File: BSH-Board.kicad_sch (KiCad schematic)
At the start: 57 parts, among them J1 667101210103, J2 MICRO QTZB5.0, SW1 TS-3025-B-C-B, SW2 TS-3025-B-C-B, U1 ESP32-C6-MINI-1-N4, U2 AP63203WU, U3 NCP715SQ50T2G, U4 TXS0102DQER

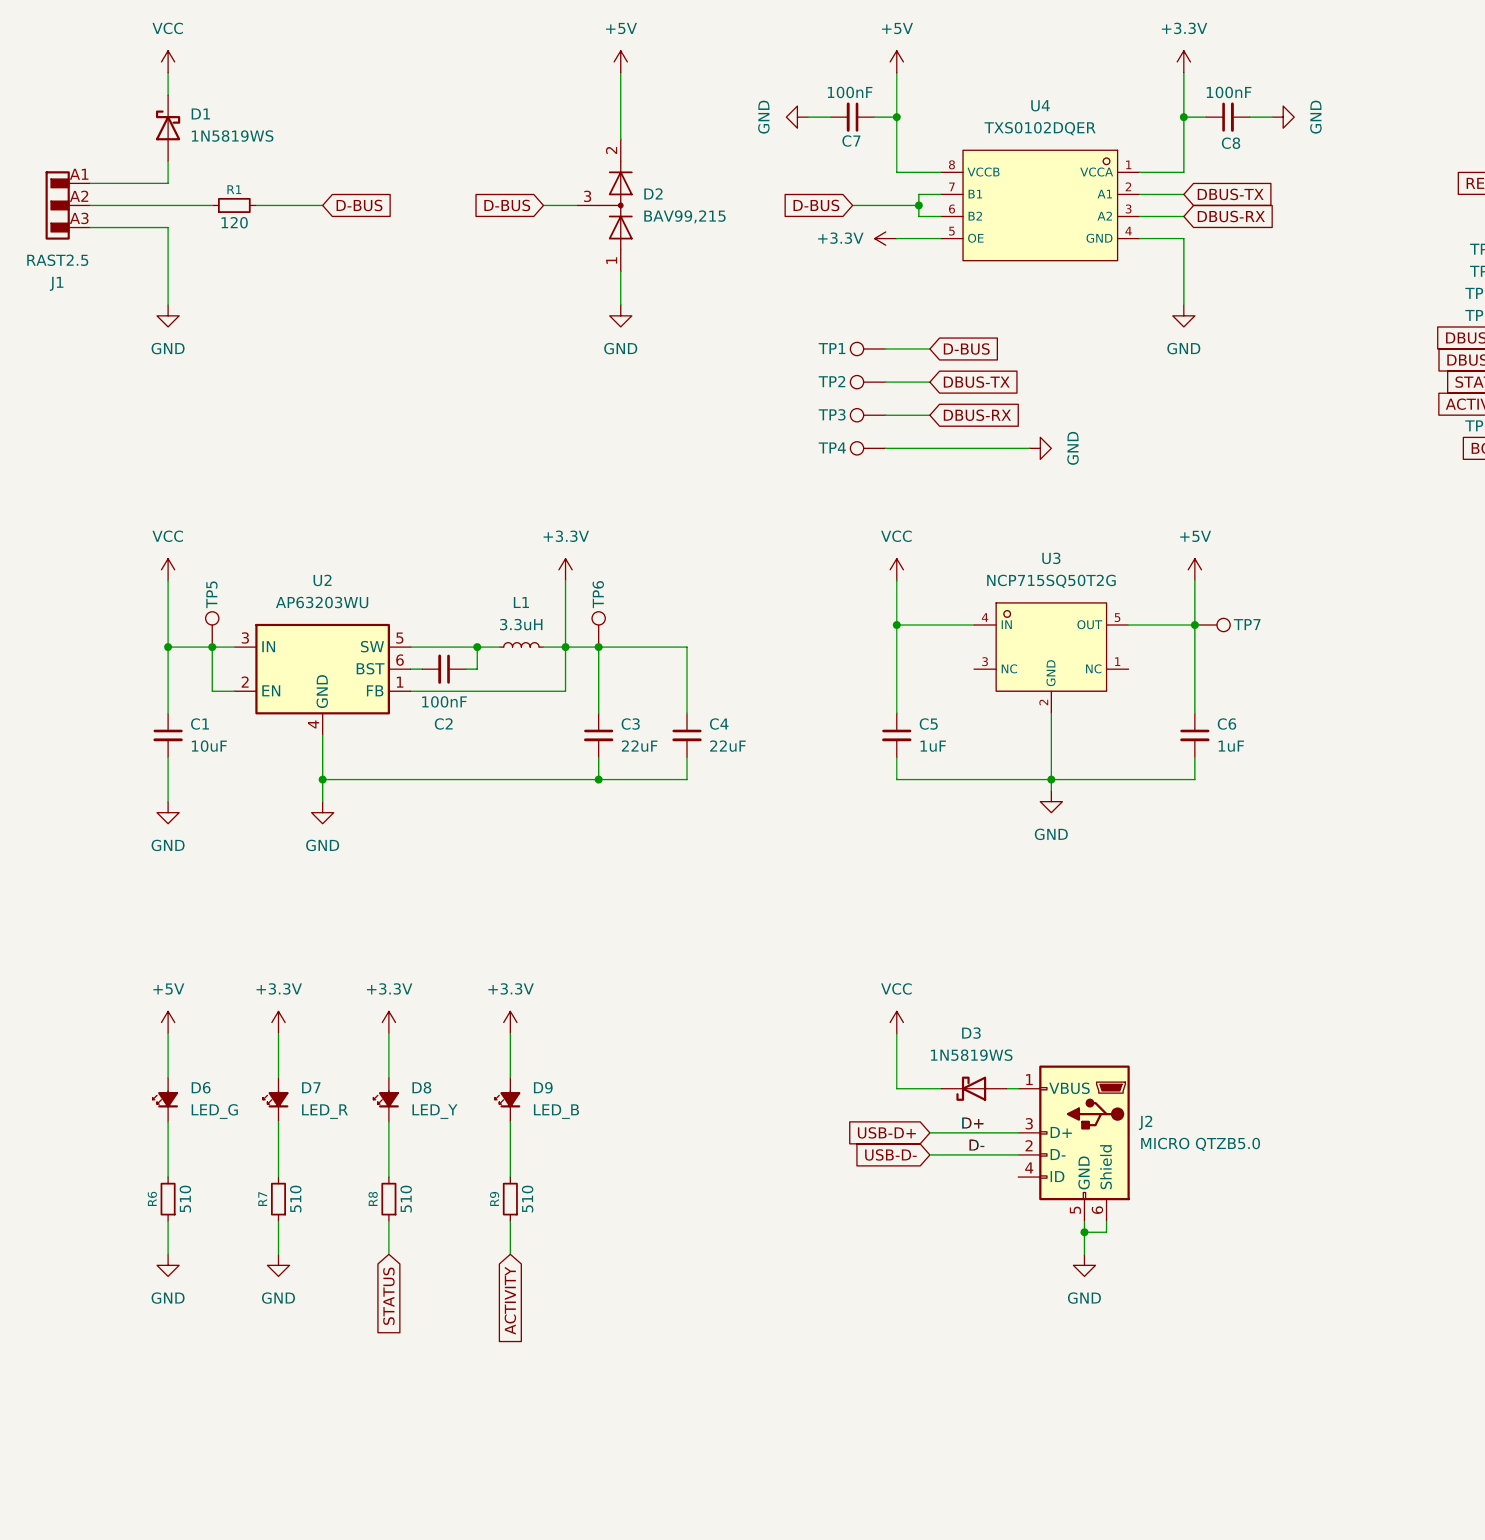
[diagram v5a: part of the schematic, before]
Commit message: Replaced TXS0102 with Pullup + 74LVC1G07 + Zener
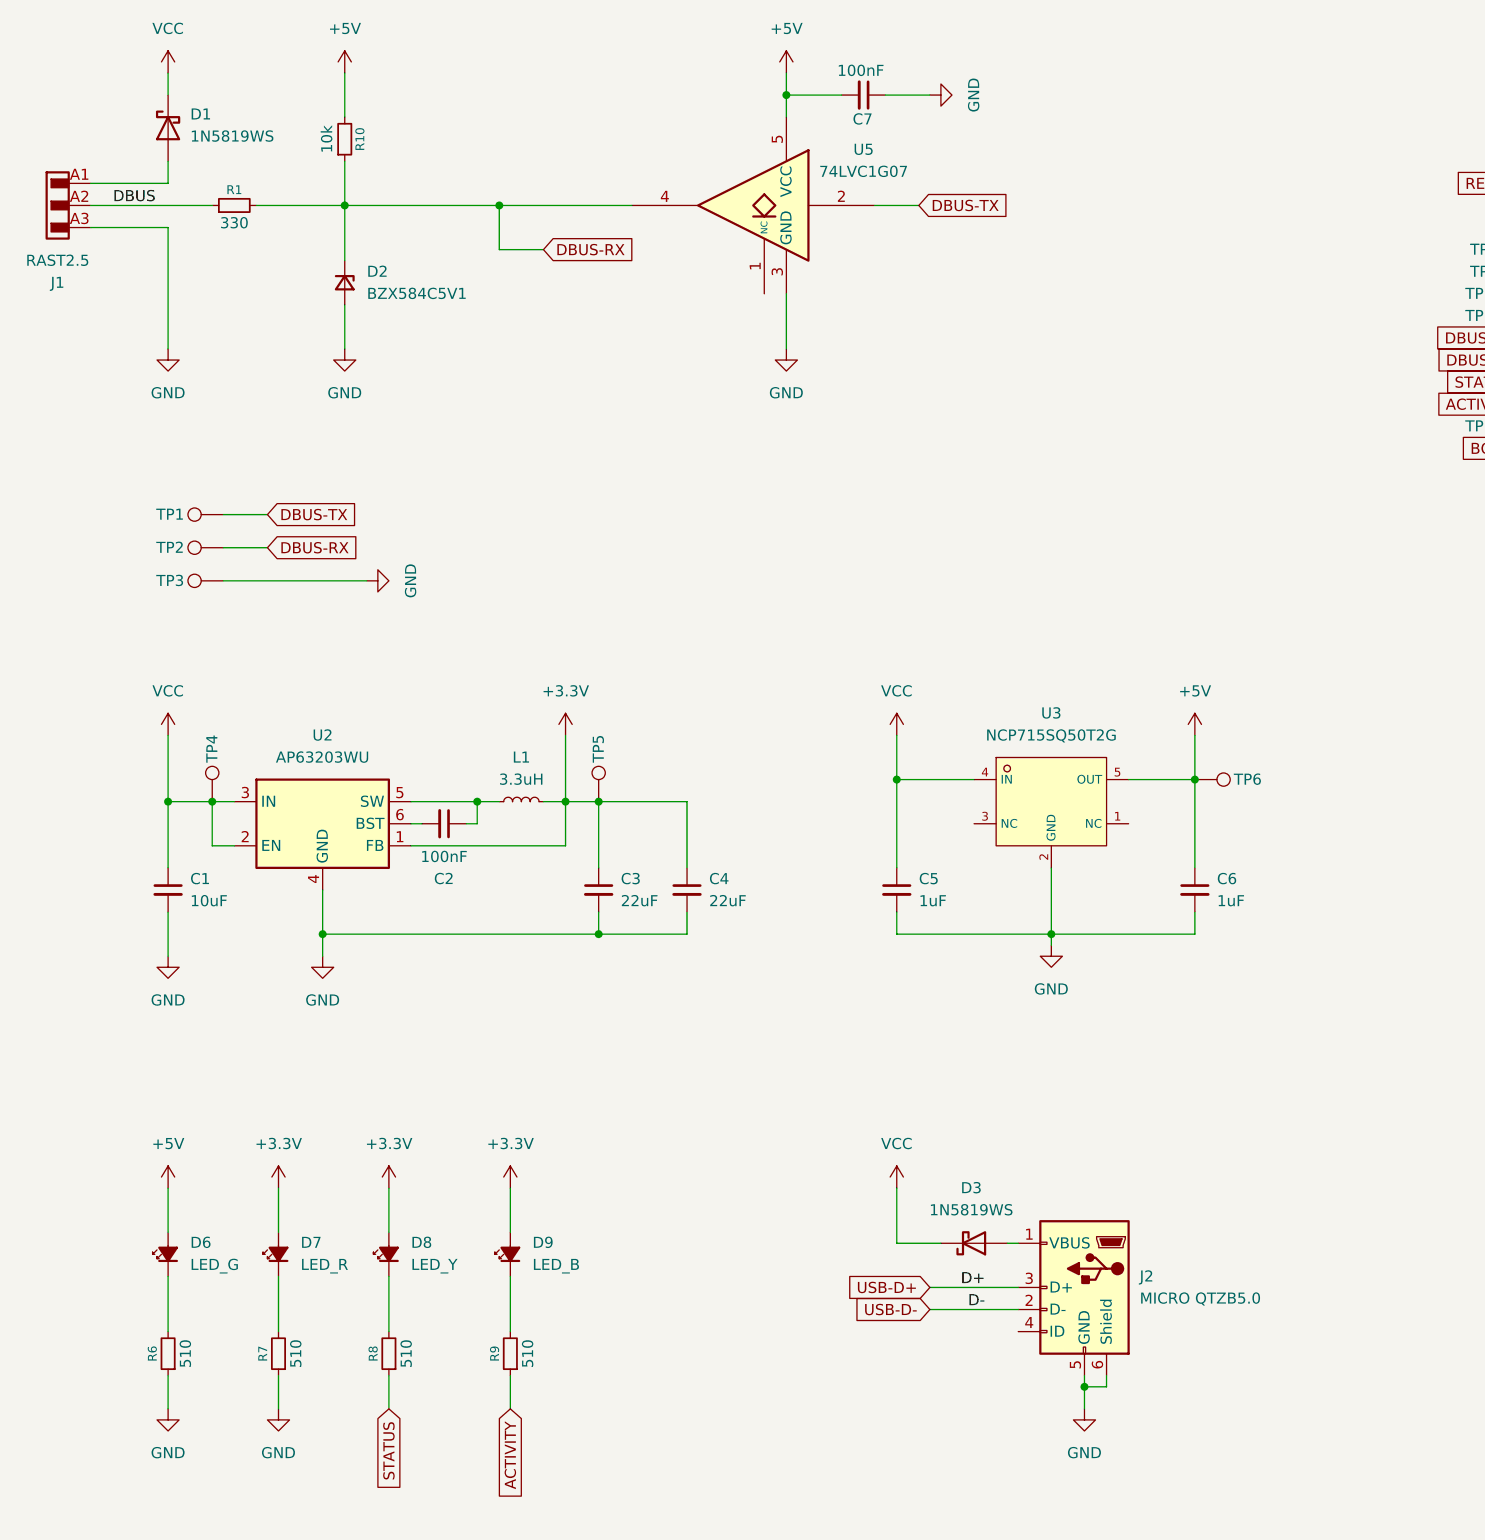
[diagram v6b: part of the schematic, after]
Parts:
- removed C8: 100nF, Capacitor_SMD:C_0402_1005Metric, symbol Device:C_Small
- removed D2: BAV99,215, Package_TO_SOT_SMD:SOT-23, symbol Diode:BAV99
- removed TP1: TestPoint, Testpoints:TestPoint_Pad_D1.0mm, symbol Connector:TestPoint
- removed U4: TXS0102DQER, footprints:X2SON-8_L1.4-W1.0-P0.35-BL, symbol TXS0102DQER:TXS0102DQER
- added D2: BZX584C5V1, Diode_SMD:D_SOD-523, symbol Device:D_Zener_Small
- added R10: 10k, Resistor_SMD:R_0402_1005Metric, symbol Device:R_Small
- added U5: 74LVC1G07, Package_TO_SOT_SMD:Diodes_SOT-553, symbol 74xGxx:74LVC1G07
- R1: value 120 -> 330; LCSC C25079 -> C25104
- renumbered TP2 to TP1, TP3 to TP2, TP4 to TP3, TP5 to TP4, TP6 to TP5, TP7 to TP6
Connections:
- net D-BUS is gone; now on net DBUS-RX: R1.2
- net +5V: now also C7.2, R10.2, U5.5 (VCC); no longer C7.1
- net DBUS-RX: now also D2.1 (K), R10.1, U5.4
- net DBUS-TX: now also U5.2
- net GND: now also C7.1, D2.2 (A), U5.3 (GND); no longer C7.2
- net DBUS: now reaches J1.A2, J1.B2, R1.1
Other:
- moved on the sheet: C1, C2, C3, C4, C5, C6, C7, D3, D6, D7, D8, D9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

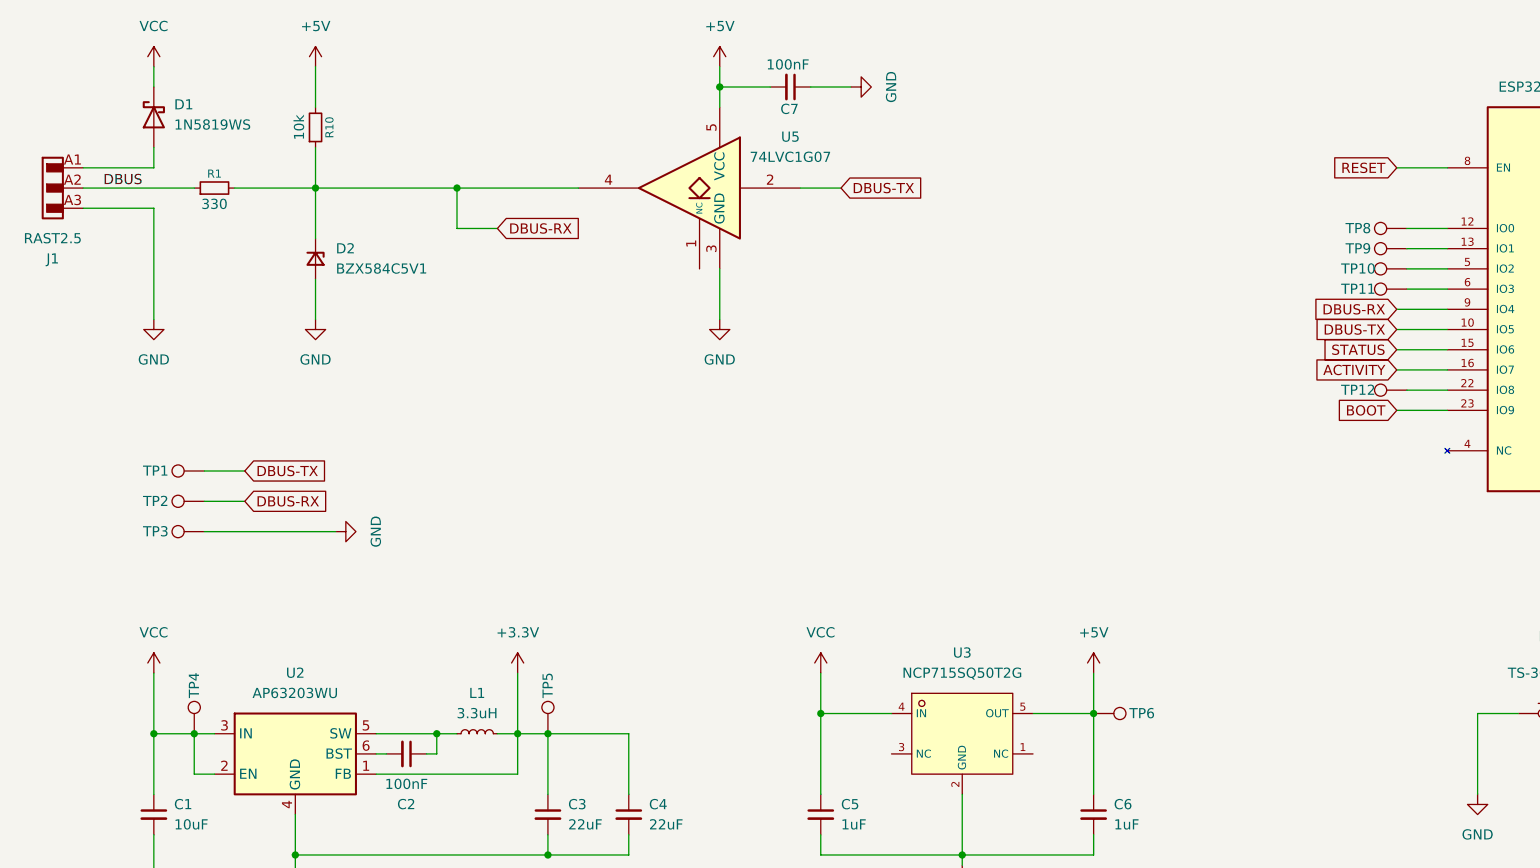
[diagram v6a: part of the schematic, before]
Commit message: Went back to LSF0102
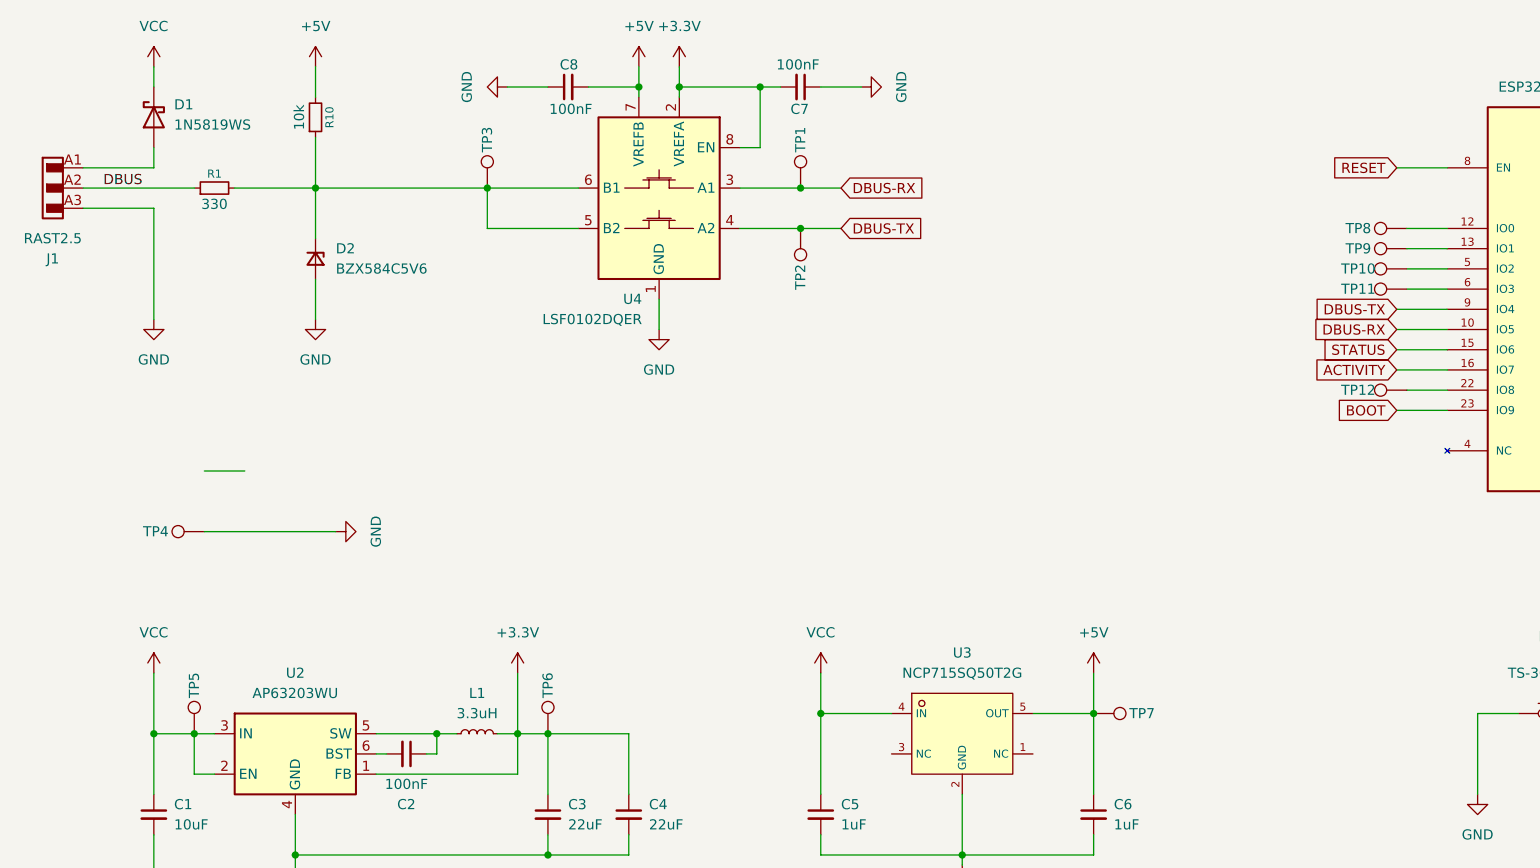
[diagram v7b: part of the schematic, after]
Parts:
- removed U5: 74LVC1G07, Package_TO_SOT_SMD:Diodes_SOT-553, symbol 74xGxx:74LVC1G07
- added C8: 100nF, Capacitor_SMD:C_0402_1005Metric, symbol Device:C_Small
- added TP2: TestPoint, Testpoints:TestPoint_Pad_D1.0mm, symbol Connector:TestPoint
- added U4: LSF0102DQER, Package_SON:X2SON-8_1.4x1mm_P0.35mm, symbol LSF0102DQER:LSF0102DQER
- D2: value BZX584C5V1 -> BZX584C5V6; LCSC C19077463 -> C19077464
- renumbered TP2 to TP3, TP3 to TP4, TP4 to TP5, TP5 to TP6, TP6 to TP7
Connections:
- net +3.3V: now also C7.2, U4.2 (VREFA), U4.8 (EN)
- net +5V: now also C8.2, U4.7 (VREFB); no longer C7.2
- net DBUS-RX: now also TP1.1, U1.10 (IO5), U4.3 (A1); no longer D2.1 (K), R1.2, R10.1, TP3.1, U1.9 (IO4)
- net DBUS-TX: now also U1.9 (IO4), TP2.1, U4.4 (A2); no longer TP1.1, U1.10 (IO5)
- net GND: now also C8.1, U4.1 (GND)
- new net: D2.1 (K), R1.2, R10.1, TP3.1, U4.5 (B2), U4.6 (B1)
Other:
- moved on the sheet: C7, TP1, TP3
